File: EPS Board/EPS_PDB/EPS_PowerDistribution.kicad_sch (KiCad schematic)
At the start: 73 parts, among them U10 TPS259621DDAT_5V_PAY, U11 LM5000-3MTCX, U12 TPS259621DDAT_5V_EPS, U13 TPS259621DDAT_5V_OBC, U14 AD7708BRUZ, U15 TPS259621DDAT_5V_ADCS, U16 TPS259621DDAT_5V_COMM, U17 LTC3624EMSE-3.3PBF, U18 TPS259621DDAT_12V_ADCS, U19 LTC3624IDD-25PBF, U6 TS4061BICT-1.25, U7 TPS259621DDAT 3V3_ADCS, U8 TPS259621DDAT_3V3_ANT, U9 TPS259621DDAT_3V3_EPS, Y2 32.768kHz

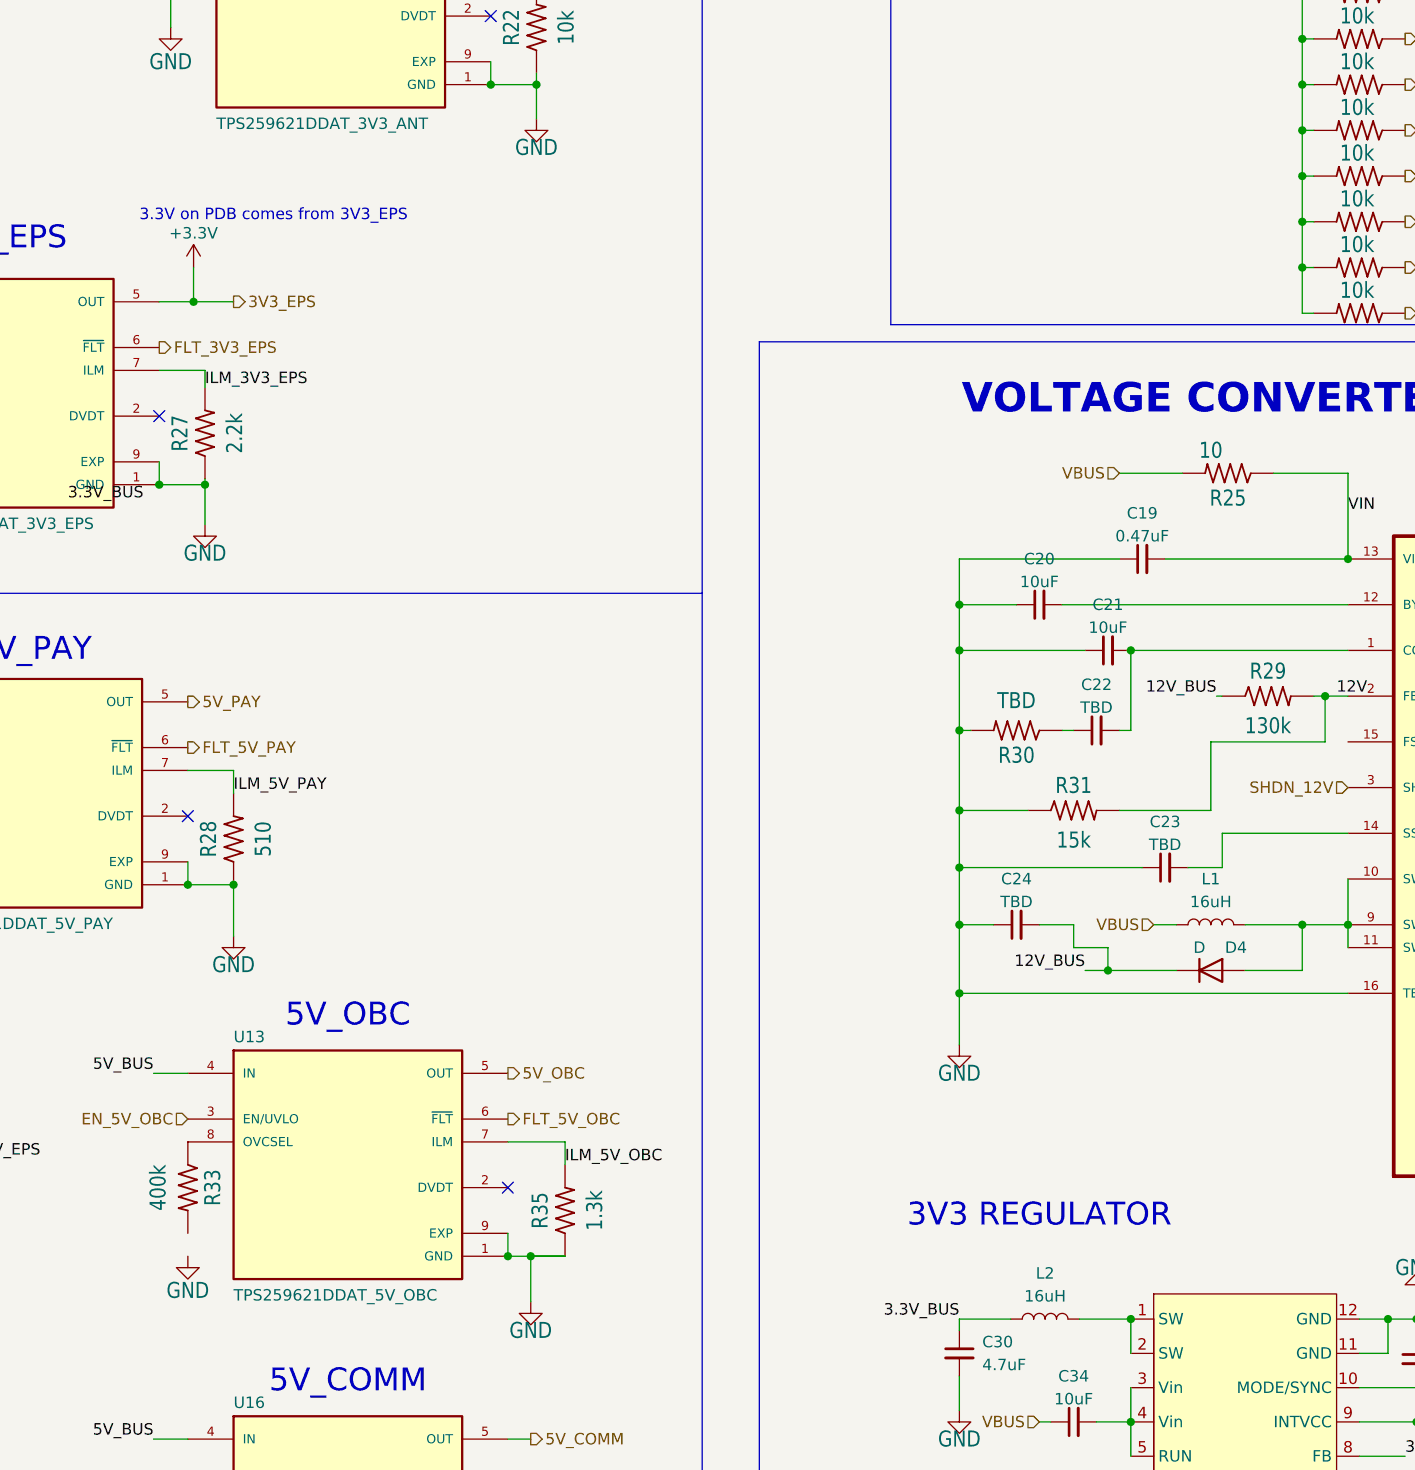
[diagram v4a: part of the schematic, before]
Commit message: Progresss in EPS PDB Layout
Voltage Converters and Current limiter section pending
Might need to increase trace width of power traces on inner layers
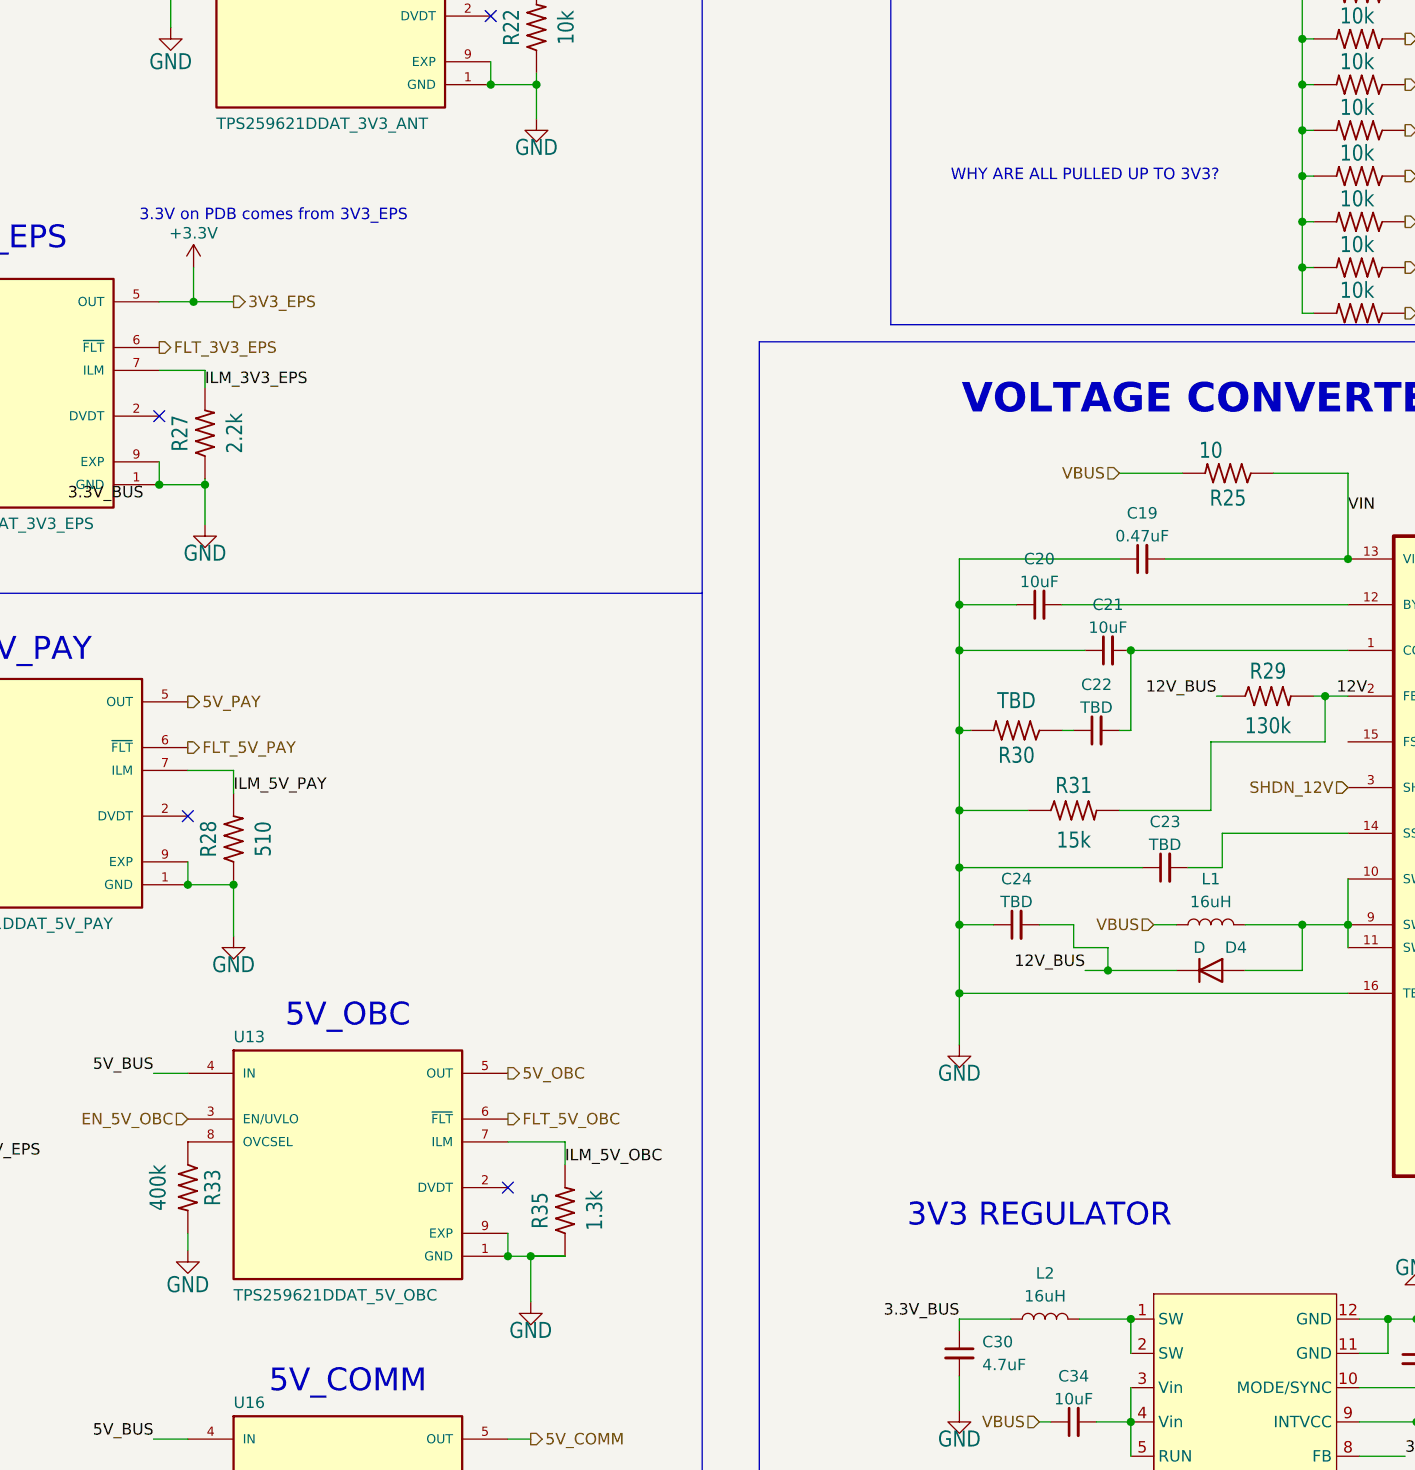
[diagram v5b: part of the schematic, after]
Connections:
- net GND: now also R33.2
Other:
- note added: "WHY ARE ALL PULLED UP TO 3V3?"
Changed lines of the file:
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@@
 	(wire
 		(pts
+			(xy 116.205 213.36) (xy 116.205 211.455)
+		)
+		(stroke
+			(width 0)
+			(type default)
+		)
+	)
+	(wire
+		(pts
 			(xy 339.725 192.405) (xy 339.725 190.5)
 		)
@@
 		)
 	)
+	(text "WHY ARE ALL PULLED UP TO 3V3?"
+		(exclude_from_sim no)
+		(at 215.9 93.98 0)
+		(effects
+			(font
+				(size 1.27 1.27)
+			)
+		)
+	)
 	(text "VIN = 7.4 V\nVOUT = 3.3 V\nIOUT (Max) = 2A\nIOUT (Min) = 0A\nf = 2.25 MHz"
 		(exclude_from_sim no)
@@
 	(symbol
 		(lib_id "power:GND")
-		(at 116.205 213.995 0)
+		(at 116.205 213.36 0)
 		(unit 1)
 		(exclude_from_sim no)
@@
 		(dnp no)
 		(property "Reference" "#SUPPLY013"
-			(at 116.205 213.995 0)
+			(at 116.205 213.36 0)
 			(effects
 				(font
@@
 		)
 		(property "Value" "GND"
-			(at 116.205 217.805 0)
+			(at 116.205 217.17 0)
 			(effects
 				(font
@@
 		)
 		(property "Footprint" ""
-			(at 116.205 213.995 0)
+			(at 116.205 213.36 0)
 			(effects
 				(font
@@
 		)
 		(property "Datasheet" ""
-			(at 116.205 213.995 0)
+			(at 116.205 213.36 0)
 			(effects
 				(font
@@
 		)
 		(property "Description" "Power symbol creates a global label with name \"GND\" , ground"
-			(at 116.205 213.995 0)
+			(at 116.205 213.36 0)
 			(effects
 				(font

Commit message: EPS PDB Layout Progress
Voltage Converter layout pending
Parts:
- L1, L2: footprint Inductor_SMD:L_Wuerth_WE-XHMI-8080 -> Inductor-WE-XHMI-5050:WE-XHMI-5050
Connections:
- net GNDA is gone; now on net GND: U14.12 (AINCOM), U14.17 (AGND_2), U14.4 (AGND)
- net GND: now also C34.1, C36.1
- net VBUS: now also C34.2, C36.2, U17.3 (Vin), U17.4 (Vin), U17.5 (RUN), U19.2 (VIN), U19.3 (RUN); no longer C34.1, C36.1
- net at C37.2, JP5.3 (B), U19.6 (INTVCC): no longer JP5.2 (C), U19.7 (MODE/SYNC)
- new net: JP5.2 (C), U19.7 (MODE/SYNC)
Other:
- note added: "ADD DECOPULING CAPS"
- note removed: "WHY ARE ALL PULLED UP TO 3V3?"
- moved on the sheet: C30, C33, C34, C35, C36, C37, JP3, JP5, L3, U19

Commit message: Assigned values to passives of 12V regulator
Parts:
- added C38, C39: 4.7uF, Capacitor_SMD:C_0603_1608Metric, symbol Device:C_Small
- C20: value 10uF -> 0.1uF
- C21: value 10uF -> 100pF
- C22: value TBD -> 3300pF
- C23: value TBD -> 10nF
- C24: value TBD -> 4.7uF
- C30: value 4.7uF -> 47uF
- L1: value 16uH -> 8.2uH
- L2: value 16uH -> 2uH
- L3: value 1.3uH -> 0.9uH
- R30: value TBD -> 18k
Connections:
- net 12V_BUS: now also C39.2
- net GND: now also C38.1, C39.1
- net VBUS: now also C38.2
- net MODE: no longer names the net of JP3.2 (C), U17.10 (MODE/SYNC)
- no-connect marks 15 -> 16
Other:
- note added: "Externall pull up PGOOD"
- note added: "L = (5/2.25*0.8)(1-(5/7.4)) L = 0.90 uH"
- note added: "REPLACE INDUCTORS WITH STANDARD VALUES PACKAGES: XHMI SERIES 8080 4.7uH 6030 8.2uH 5050 15.6uH"
- note added: "VIN = 7.4 V VOUT = 3.3 V IOUT (Max) = 1A IOUT (Min) = 0A f = 2.25 MHz"
- note added: "VIN = 7.4 V VOUT = 5 V IOUT (Max) = 2A IOUT (Min) = 0A f = 2.25 MHz"
- note removed: "REPLACE INDUCTORS WITH STANDARD VALUES PACKAGES: XHMI SERIES 4.7uH 6030 8.2uH 5050 15.6uH"
- note removed: "VIN = 7.4 V VOUT = 3.3 V IOUT (Max) = 2A IOUT (Min) = 0A f = 2.25 MHz"
- moved on the sheet: C19, C20, C21, C22, C23, C24, C36, D4, L1, R25, R29, R30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

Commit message: Added decoupling caps to current limiters
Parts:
- added C40, C41, C42, C43, C44, C45, C46, C47, C48: 1uF, Capacitor_SMD:C_0603_1608Metric, symbol Device:C_Small
- added D6: D_Schottky, Diode_SMD:D_0805_2012Metric, symbol Device:D_Schottky
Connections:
- net +3.3V: now also C42.2
- net 12V_ADCS: now also C48.2
- net 3V3_ADCS: now also C40.2
- net 3V3_ANT: now also C41.2
- net 5V_ADCS: now also C46.2
- net 5V_COMM: now also C47.2
- net 5V_EPS: now also C44.2, D6.1 (K)
- net 5V_OBC: now also C45.2
- net 5V_PAY: now also C43.2
- net GND: now also C40.1, C41.1, C42.1, C43.1, C44.1, C45.1, C46.1, C47.1, C48.1, D6.2 (A)
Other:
- note removed: "ADD DECOPULING CAPS"
- moved on the sheet: D3
